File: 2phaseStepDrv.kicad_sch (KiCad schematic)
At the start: 18 parts

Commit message: ver0
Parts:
- added J?: (no value), symbol Connector:Screw_Terminal_01x06
- added U?: (no value), symbol 4xxx:4028
- J? (x2): value (none) -> Screw_Terminal_01x02
- Q? (x8): value (none) -> BC338; footprint (none) -> Package_TO_SOT_THT:TO-92_Inline
- R?: value (none) -> R
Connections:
- net +12V: now also Q?.1 (C), Q?.1 (C), Q?.1 (C), Q?.1 (C), J?.5 (Pin_5), U?.16 (VDD)
- net Earth: now also J?.6 (Pin_6), U?.11 (D), U?.8 (VSS)
- net at R?.2, R?.2: now also U?.3 (S0)
- net at R?.2, R?.2: now also U?.2 (S2)
- net at R?.2, R?.2: now also U?.15 (S3)
- net at R?.2, R?.2: now also U?.14 (S1)
- new net: J?.1 (Pin_1), U?.10 (A)
- new net: J?.3 (Pin_3), U?.12 (C)
- new net: J?.2 (Pin_2), U?.13 (B)

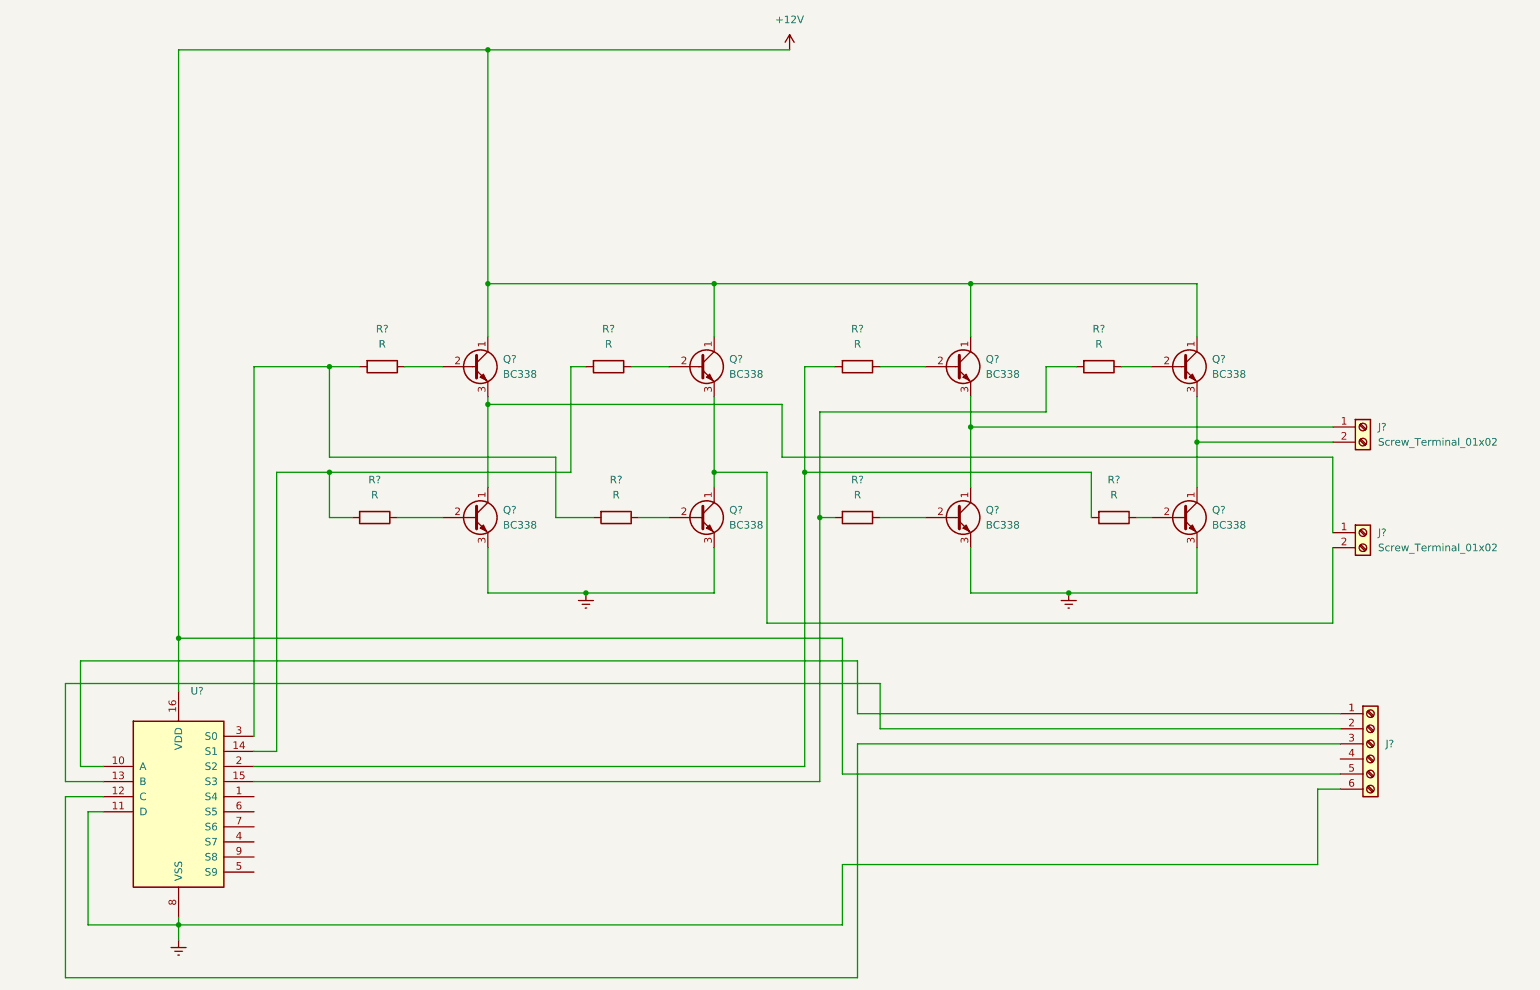
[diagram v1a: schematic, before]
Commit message: Changed devices and included foot-prints
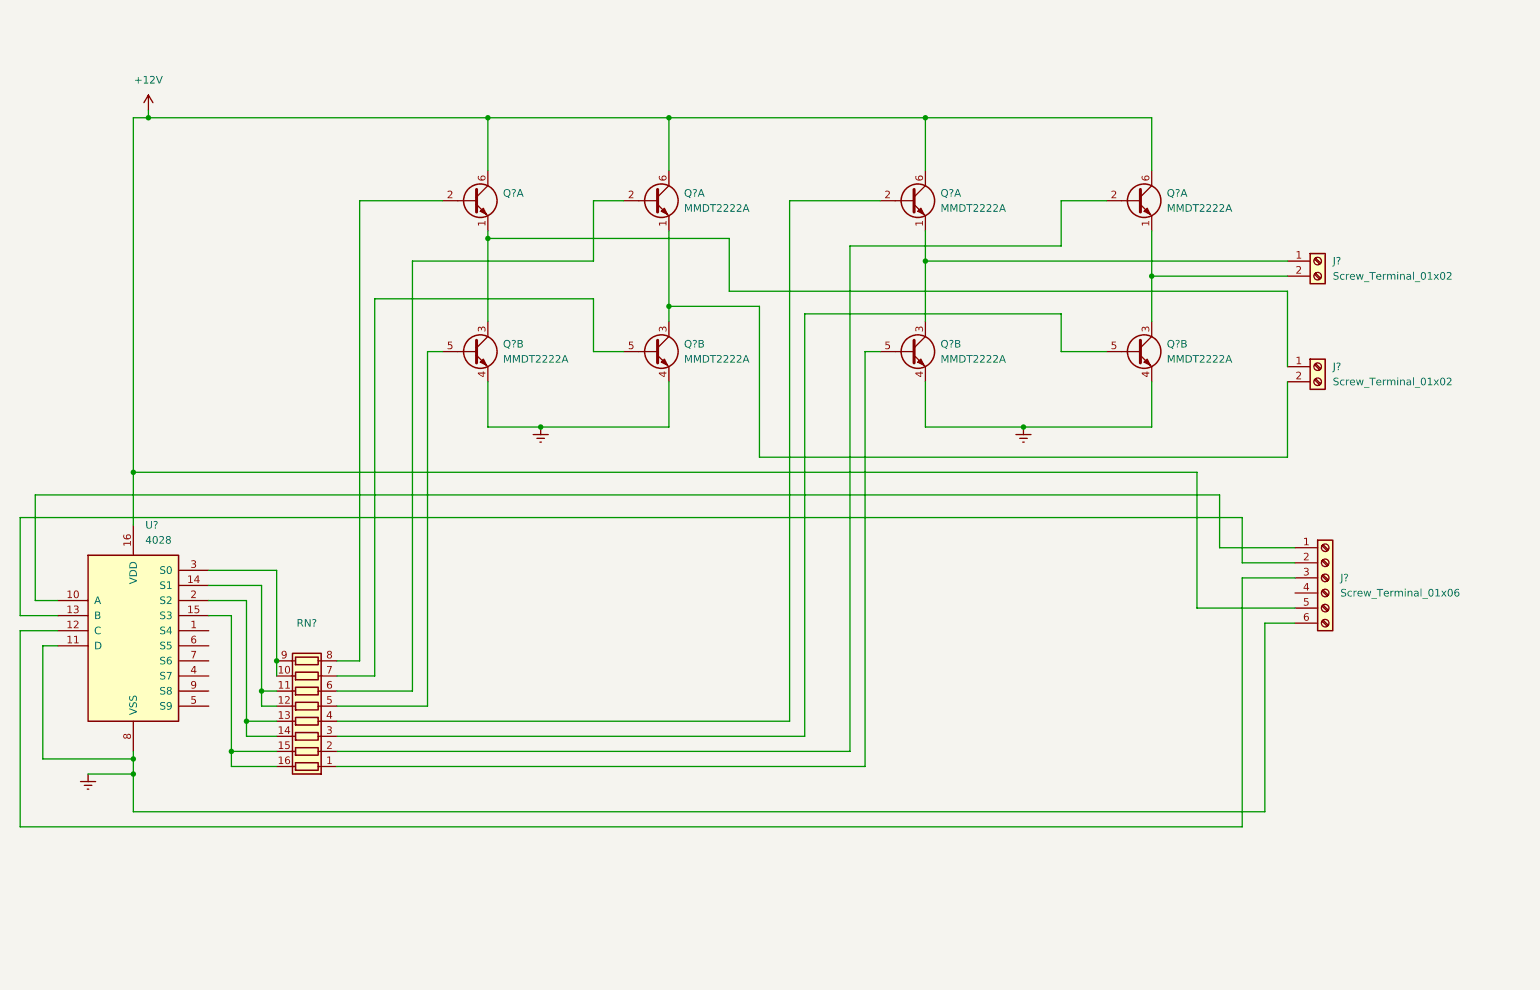
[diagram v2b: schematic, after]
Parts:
- removed Q? (x8): BC338, Package_TO_SOT_THT:TO-92_Inline, symbol Transistor_BJT:BC338
- removed R? (x8): R, symbol Device:R
- added Q? (x7): MMDT2222A, Package_TO_SOT_SMD:SOT-363_SC-70-6, symbol Transistor_BJT:MMDT2222A
- added Q?: (no value), symbol Transistor_BJT:MMDT2222A
- added RN?: (no value), symbol Device:R_Pack08
- J?: value (none) -> Screw_Terminal_01x06
- U?: value (none) -> 4028
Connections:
- net +12V: now also Q?.6 (C1), Q?.6 (C1), Q?.6 (C1), Q?.6 (C1)
- net Earth: now also Q?.4 (E2), Q?.4 (E2), Q?.4 (E2), Q?.4 (E2)
- net at J?.2 (Pin_2): now also Q?.1 (E1), Q?.3 (C2) (x2)
- net at J?.1 (Pin_1): now also Q?.1 (E1), Q?.3 (C2) (x2)
- net at U?.14 (S1): now also RN?.11 (R6.2), RN?.12 (R5.2)
- net at U?.15 (S3): now also RN?.15 (R2.2), RN?.16 (R1.2)
- net at U?.2 (S2): now also RN?.13 (R4.2), RN?.14 (R3.2)
- net at U?.3 (S0): now also RN?.10 (R7.2), RN?.9 (R8.2)
- new net: Q?.5 (B2), RN?.1 (R1.1)
- new net: Q?.2 (B1), RN?.2 (R2.1)
- new net: Q?.5 (B2), RN?.3 (R3.1)
- new net: Q?.2 (B1), RN?.4 (R4.1)
- new net: Q?.5 (B2), RN?.5 (R5.1)
- new net: Q?.2 (B1), RN?.6 (R6.1)
- new net: Q?.5 (B2), RN?.7 (R7.1)
- new net: Q?.2 (B1), RN?.8 (R8.1)
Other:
- moved on the sheet: J?, U?

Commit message: new footprints and diodes
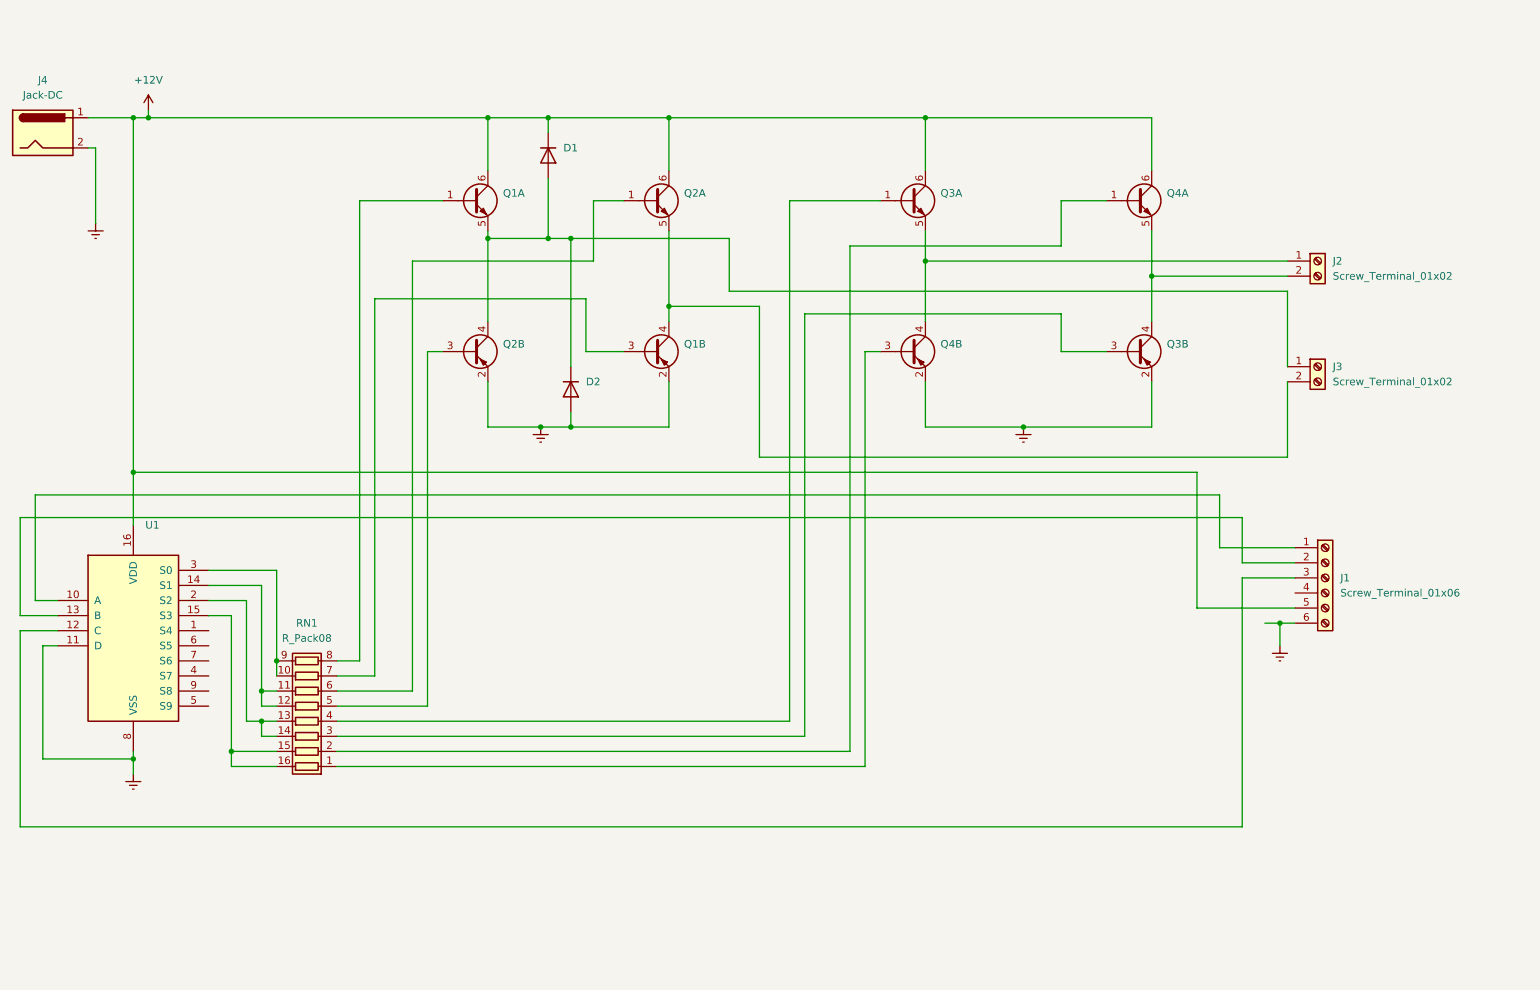
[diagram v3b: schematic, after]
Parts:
- removed Q? (x7): MMDT2222A, Package_TO_SOT_SMD:SOT-363_SC-70-6, symbol Transistor_BJT:MMDT2222A
- removed Q?: (no value), symbol Transistor_BJT:MMDT2222A
- added D1, D2: (no value), symbol Diode:1N4149
- added J4: Jack-DC, Connector_BarrelJack:BarrelJack_Wuerth_6941xx301002, symbol Connector:Jack-DC
- added Q1, Q2, Q3, Q4: (no value), symbol Transistor_BJT:FMB2227A
- J1: renamed from J?; footprint (none) -> TerminalBlock:TerminalBlock_bornier-6_P5.08mm
- J2, J3: renamed from J?; footprint (none) -> TerminalBlock:TerminalBlock_bornier-2_P5.08mm
- RN1: renamed from RN?; value (none) -> R_Pack08; footprint (none) -> Package_SO:SOIC-16_4.55x10.3mm_P1.27mm
- U1: renamed from U?; value 4028 -> (none)
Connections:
- net +12V: now also D1.1 (K), J4.1, Q1.6 (C1), Q2.6 (C1), Q3.6 (C1), Q4.6 (C1)
- net Earth: now also D2.2 (A), J4.2, Q1.2 (E2), Q2.2 (E2), Q3.2 (E2), Q4.2 (E2)
- net at J3.1 (Pin_1): now also D1.2 (A), D2.1 (K), Q1.5 (E1), Q2.4 (C2)
- net at J3.2 (Pin_2): now also Q1.4 (C2), Q2.5 (E1)
- net at J2.1 (Pin_1): now also Q3.5 (E1), Q4.4 (C2)
- net at RN1.1 (R1.1): now also Q4.3 (B2)
- net at RN1.2 (R2.1): now also Q4.1 (B1)
- net at RN1.3 (R3.1): now also Q3.3 (B2)
- net at RN1.4 (R4.1): now also Q3.1 (B1)
- net at RN1.5 (R5.1): now also Q2.3 (B2)
- net at RN1.6 (R6.1): now also Q2.1 (B1)
- net at RN1.7 (R7.1): now also Q1.3 (B2)
- net at RN1.8 (R8.1): now also Q1.1 (B1)
- net at J2.2 (Pin_2): now also Q3.4 (C2), Q4.5 (E1)

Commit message: Updated transistors, added flybacks and adjusted foor-prints
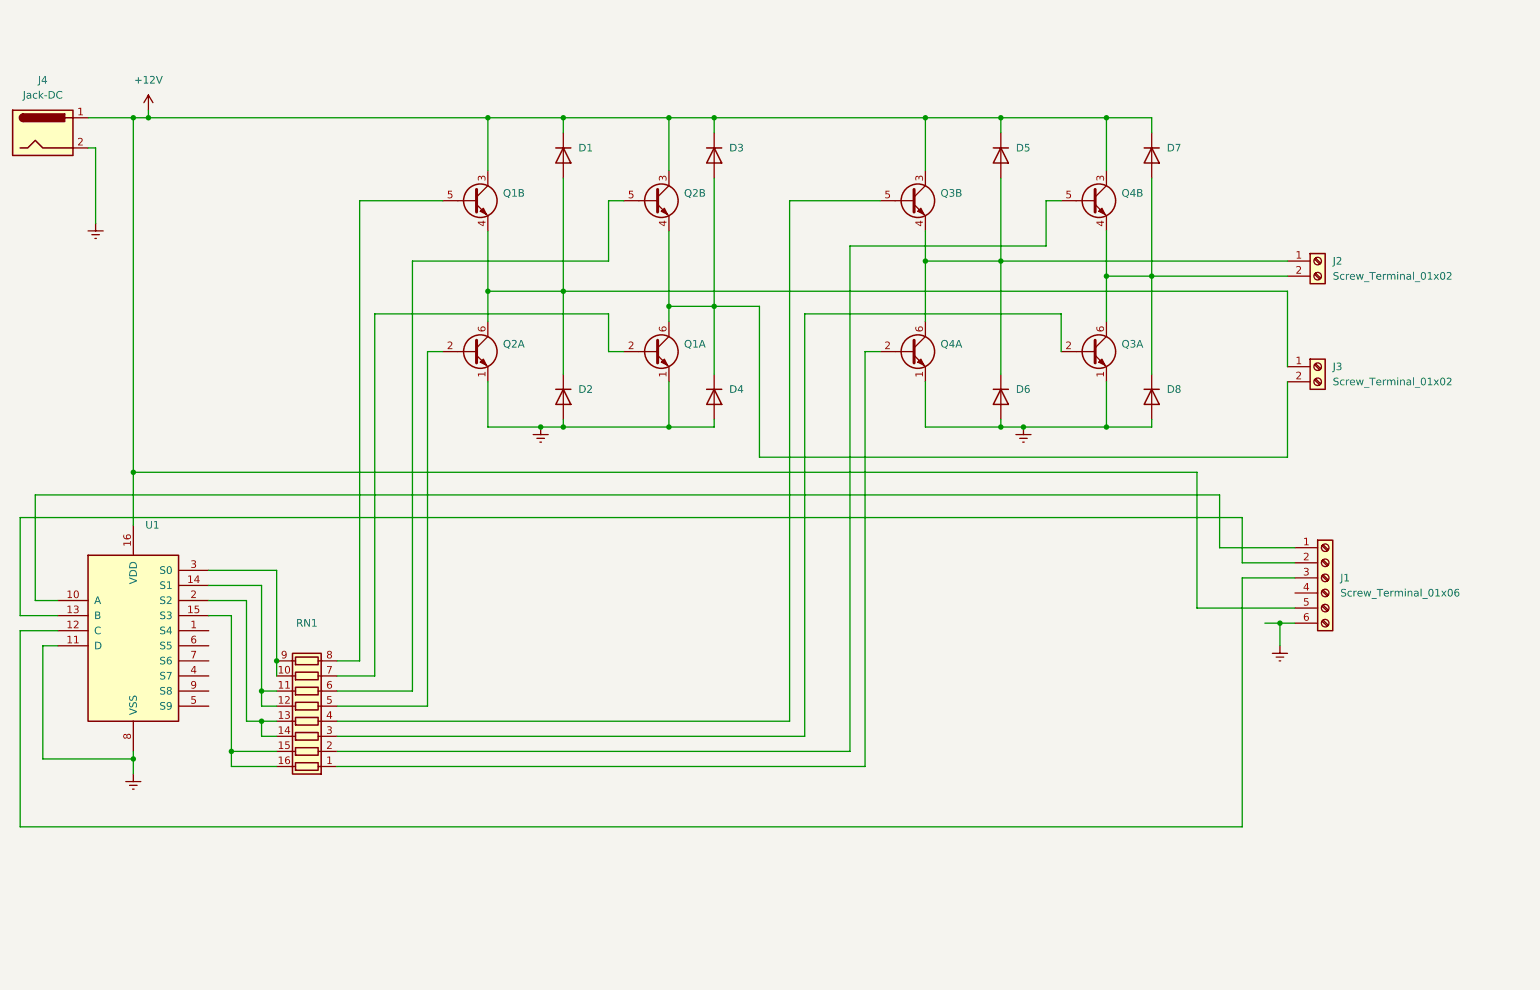
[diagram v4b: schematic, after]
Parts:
- removed Q1, Q2, Q3, Q4: (no value), symbol Transistor_BJT:FMB2227A
- added D3, D4, D5, D6, D7, D8: (no value), symbol Diode:1N4149
- added Q1, Q2, Q3, Q4: (no value), symbol Transistor_BJT:MBT2222ADW1T1
- RN1: value R_Pack08 -> (none); footprint Package_SO:SOIC-16_4.55x10.3mm_P1.27mm -> (none)
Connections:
- net +12V: now also D3.1 (K), D5.1 (K), D7.1 (K), Q1.3 (C2), Q2.3 (C2), Q3.3 (C2), Q4.3 (C2)
- net Earth: now also D4.2 (A), D6.2 (A), D8.2 (A), Q1.1 (E1), Q2.1 (E1), Q3.1 (E1), Q4.1 (E1)
- net at RN1.8 (R8.1): now also Q1.5 (B2)
- net at D1.2 (A), D2.1 (K), J3.1 (Pin_1): now also Q1.4 (E2), Q2.6 (C1)
- net at J3.2 (Pin_2): now also D3.2 (A), D4.1 (K), Q1.6 (C1), Q2.4 (E2)
- net at RN1.1 (R1.1): now also Q4.2 (B1)
- net at RN1.2 (R2.1): now also Q4.5 (B2)
- net at RN1.3 (R3.1): now also Q3.2 (B1)
- net at RN1.4 (R4.1): now also Q3.5 (B2)
- net at RN1.5 (R5.1): now also Q2.2 (B1)
- net at RN1.6 (R6.1): now also Q2.5 (B2)
- net at RN1.7 (R7.1): now also Q1.2 (B1)
- net at J2.2 (Pin_2): now also D7.2 (A), D8.1 (K), Q3.6 (C1), Q4.4 (E2)
- net at J2.1 (Pin_1): now also D5.2 (A), D6.1 (K), Q3.4 (E2), Q4.6 (C1)
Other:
- moved on the sheet: D1, D2
